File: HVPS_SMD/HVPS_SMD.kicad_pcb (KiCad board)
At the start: 2 copper layers, 36.8 x 22.9 mm, 22 parts, among them J1 CONN_01X02, J2 CONN_01X02, J3 CONN_01X02, Q1 AO4294, T1 WE-FLEX_ER11_5, U1 LM3478SOIC8

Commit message: Prepare for Fab
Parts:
- T1: value WE-FLEX_ER11_5 -> MagTop-HVSMPS
- moved R1 1.92 mm to (183.5, 66.0)
- moved R2 1.78 mm to (185.4, 66.0)
- moved D1 0.48 mm to (194.7, 63.5)
- moved R4 0.31 mm to (183.7, 71.1)
- moved C3 0.18 mm to (188.2, 65.0)
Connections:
- T1 pad 10: Net-(T1-Pad10) -> (no net)
- T1 pad 11: Net-(T1-Pad11) -> (no net)
- T1 pad 12: Net-(T1-Pad12) -> (no net)
- T1 pad 3: Net-(T1-Pad3) -> (no net)
- T1 pad 4: Net-(T1-Pad3) -> (no net)
- T1 pad 6: Net-(T1-Pad12) -> (no net)
- T1 pad 7: Net-(T1-Pad11) -> (no net)
- T1 pad 9: Net-(T1-Pad10) -> (no net)
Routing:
- net Net-(T1-Pad12): track 42.3 -> 0.00 mm
- net GND: track 27.0 -> 40.5 mm
- net Net-(T1-Pad11): track 10.7 -> 0.00 mm
- net Net-(R1-Pad2): track 1.27 -> 2.69 mm
- net Vout: track 13.3 -> 14.7 mm
- net Net-(R2-Pad2): track 28.0 -> 29.3 mm
- net Vin: track 30.6 -> 31.4 mm
- removed copper zone on F.Cu, net Net-(T1-Pad10)
- removed copper zone on F.Cu, net Net-(T1-Pad3)
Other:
- board text added: "nixies.us hvps v0.2"
- board text removed: "nixies.us hvps v0.1"

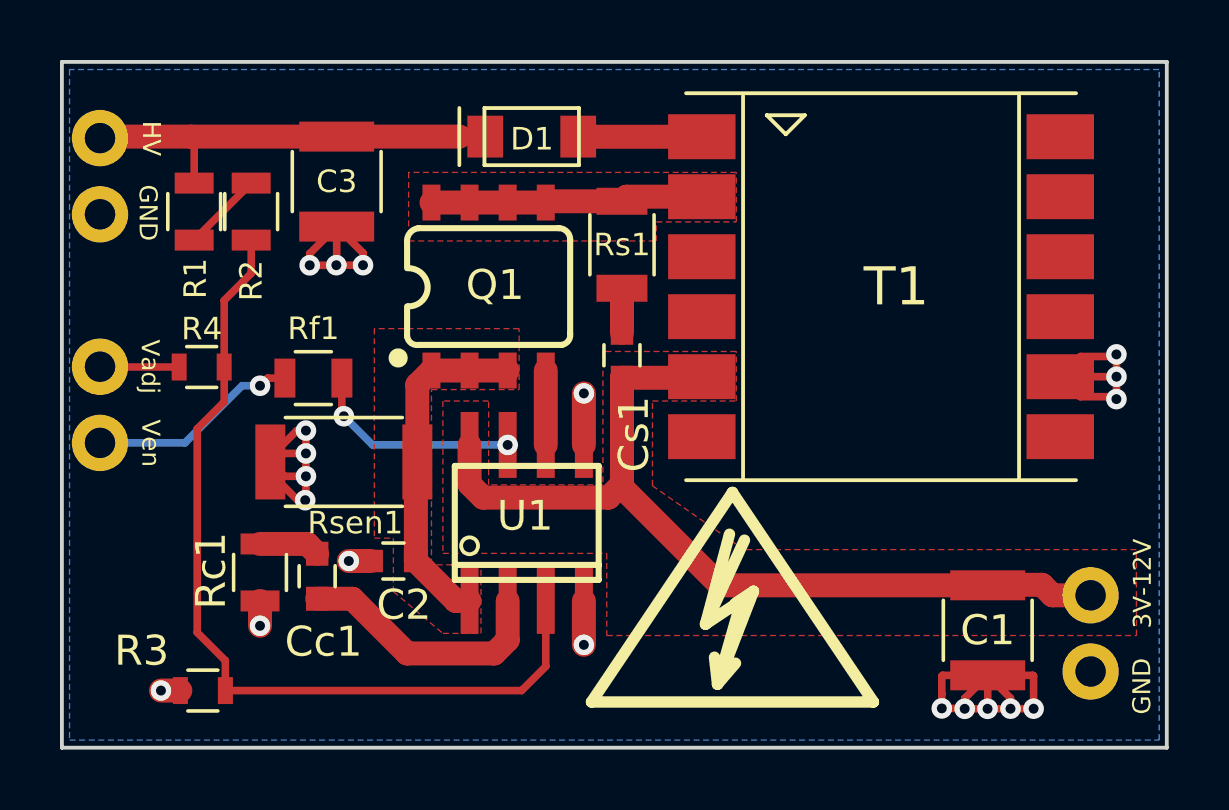
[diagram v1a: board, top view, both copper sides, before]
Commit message: Add footprint for Vfix resistor R5
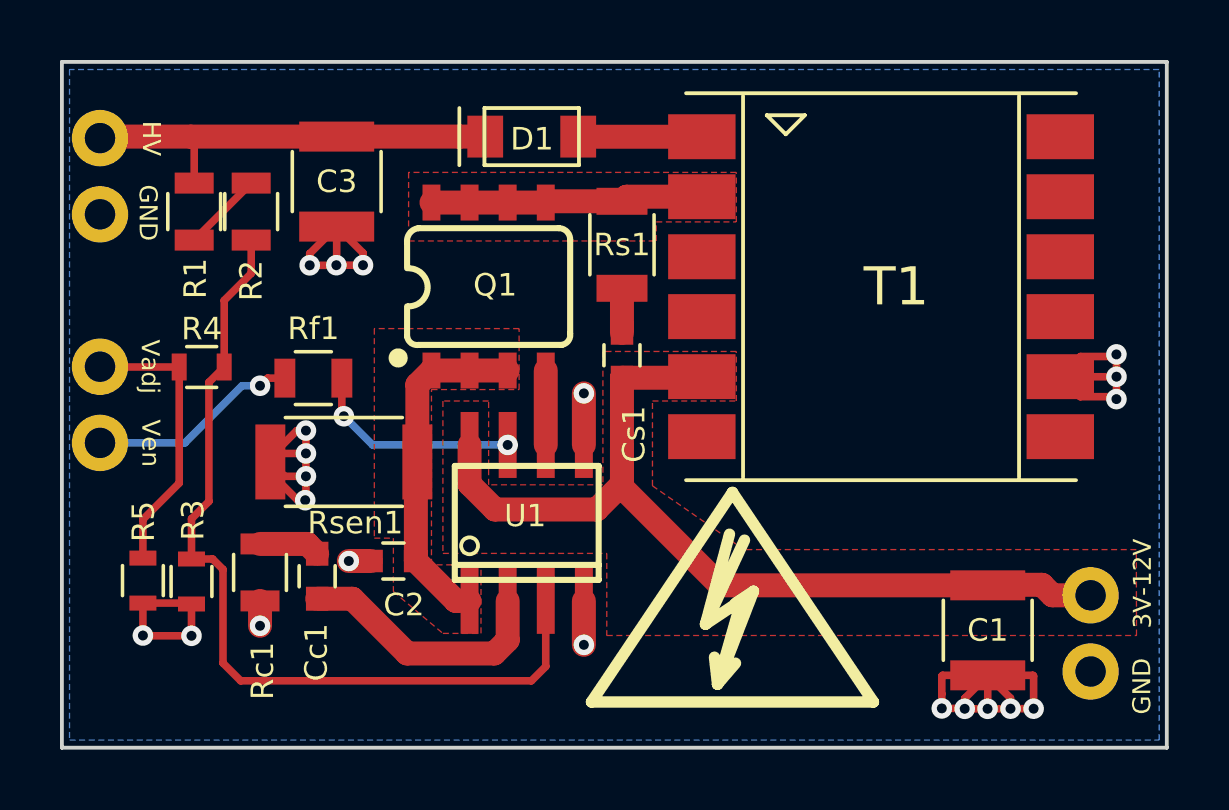
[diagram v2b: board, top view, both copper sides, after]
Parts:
- removed G***: LOGO, logos:mermaid_l
- added R5: 30k, lib_fp:R_0603, F.Cu at (181.8, 78.2)
- moved R3 3.65 mm to (183.4, 78.3), turned to 270 degrees
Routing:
- net Vadj: track 2.64 -> 9.52 mm
- net GND: track 40.5 -> 45.4 mm, vias 20 -> 21

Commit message: Prepare for fab
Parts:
- moved R4 7.39 mm to (181.9, 78.3), turned to 90 degrees
- moved R5 1.39 mm to (180.4, 78.3)
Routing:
- net Vadj: track 9.52 -> 11.5 mm
- net Net-(R2-Pad2): track 29.2 -> 30.7 mm
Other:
- board text added: "nixieclock.biz nixies.us hvps v0.2"
- board text removed: "nixies.us hvps v0.2"
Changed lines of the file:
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@@
     (thickness 1.6002)
     (drawings 11)
-    (tracks 170)
+    (tracks 171)
     (zones 0)
     (modules 22)
@@
   )
   (setup
-    (last_trace_width 0.1524)
+    (last_trace_width 0.254)
     (user_trace_width 0.1524)
     (user_trace_width 0.2)
@@
   )
   (module lib_fp:R_0603 (layer F.Cu)
-    (at 181.77 78.25 90)
+    (at 180.38 78.28 90)
     (descr "Resistor SMD 0603, reflow soldering, Vishay (see dcrcw.pdf)")
     (tags "resistor 0603")
     (attr smd)
-    (fp_text reference R5 (at 1.97 0.02 270) (layer F.SilkS)
+    (fp_text reference R5 (at 1.99 0.03 270) (layer F.SilkS)
       (effects (font (size 0.75 0.75) (thickness 0.1)))
     )
@@
   )
   (module lib_fp:R_0603 (layer F.Cu)
-    (at 183.73 71.13)
+    (at 181.88 78.28 90)
     (descr "Resistor SMD 0603, reflow soldering, Vishay (see dcrcw.pdf)")
     (tags "resistor 0603")
     (attr smd)
-    (fp_text reference R4 (at 0 -1.27 180) (layer F.SilkS)
-      (effects (font (size 0.75 0.75) (thickness 0.1)))
-    )
-    (fp_text value 30k (at 0 1.5) (layer F.Fab)
-      (effects (font (size 1 1) (thickness 0.15)))
-    )
-    (fp_text user %R (at 0 0) (layer F.Fab)
+    (fp_text reference R4 (at 2.01 -0.02 270) (layer F.SilkS)
+      (effects (font (size 0.75 0.75) (thickness 0.1)))
+    )
+    (fp_text value 30k (at 0 1.5 90) (layer F.Fab)
+      (effects (font (size 1 1) (thickness 0.15)))
+    )
+    (fp_text user %R (at 0 0 90) (layer F.Fab)
       (effects (font (size 0.4 0.4) (thickness 0.075)))
     )
@@
     (fp_line (start 1.25 0.7) (end 1.25 -0.7) (layer F.CrtYd) (width 0.05))
     (fp_line (start 1.25 0.7) (end -1.25 0.7) (layer F.CrtYd) (width 0.05))
-    (pad 1 smd rect (at -0.75 0) (size 0.5 0.9) (layers F.Cu F.Paste F.Mask)
+    (pad 1 smd rect (at -0.75 0 90) (size 0.5 0.9) (layers F.Cu F.Paste F.Mask)
       (net 6 Vadj))
-    (pad 2 smd rect (at 0.75 0) (size 0.5 0.9) (layers F.Cu F.Paste F.Mask)
+    (pad 2 smd rect (at 0.75 0 90) (size 0.5 0.9) (layers F.Cu F.Paste F.Mask)
       (net 8 "Net-(R2-Pad2)"))
     (model ${KISYS3DMOD}/Resistors_SMD.3dshapes/R_0603.wrl
@@
     (effects (font (size 0.6 0.6) (thickness 0.127)))
   )
-  (gr_text "nixies.us\nhvps v0.2" (at 204.724 80.645) (layer B.Mask)
+  (gr_text "nixieclock.biz\nnixies.us\nhvps v0.2" (at 207.02 78.95) (layer B.Mask)
     (effects (font (size 1.2 1.2) (thickness 0.254)) (justify left mirror))
   )
@@
   (via (at 189.107 67.736) (size 0.6858) (drill 0.3302) (layers F.Cu B.Cu) (net 2))
   (via (at 188.633009 77.597) (size 0.6858) (drill 0.3302) (layers F.Cu B.Cu) (net 2))
-  (segment (start 185.674 78.928) (end 185.674 79.756) (width 0.8) (layer F.Cu) (net 2))
   (via (at 185.674 79.756) (size 0.6858) (drill 0.3302) (layers F.Cu B.Cu) (net 2))
   (via (at 183.39 80.09) (size 0.6858) (drill 0.3302) (layers F.Cu B.Cu) (net 2))
@@
   (segment (start 189.369 77.597) (end 188.633009 77.597) (width 0.8) (layer F.Cu) (net 2))
   (segment (start 183.36 79) (end 183.39 79.03) (width 0.254) (layer F.Cu) (net 2))
-  (segment (start 181.77 79) (end 183.36 79) (width 0.254) (layer F.Cu) (net 2))
-  (segment (start 185.572 79.03) (end 185.674 78.928) (width 0.254) (layer F.Cu) (net 2))
-  (via (at 181.77 80.08) (size 0.6858) (drill 0.3302) (layers F.Cu B.Cu) (net 2))
-  (segment (start 181.77 79) (end 181.77 80.08) (width 0.254) (layer F.Cu) (net 2))
+  (via (at 180.39 80.09) (size 0.6858) (drill 0.3302) (layers F.Cu B.Cu) (net 2))
   (segment (start 183.39 79.03) (end 183.39 80.09) (width 0.254) (layer F.Cu) (net 2))
-  (segment (start 181.78 80.09) (end 181.77 80.08) (width 0.254) (layer F.Cu) (net 2))
-  (segment (start 183.39 80.09) (end 181.78 80.09) (width 0.254) (layer F.Cu) (net 2))
+  (segment (start 180.38 79.03) (end 180.38 80.08) (width 0.254) (layer F.Cu) (net 2))
+  (segment (start 180.39 80.09) (end 183.39 80.09) (width 0.254) (layer F.Cu) (net 2))
+  (segment (start 185.674 79.756) (end 185.674 78.928) (width 0.254) (layer F.Cu) (net 2))
   (segment (start 192.659 71.247) (end 193.929 71.247) (width 0.8) (layer F.Cu) (net 3))
   (segment (start 191.389 71.247) (end 192.659 71.247) (width 0.8) (layer F.Cu) (net 3))
@@
   (segment (start 185.928 71.501) (end 185.674 71.755) (width 0.254) (layer F.Cu) (net 5))
   (segment (start 186.502 71.501) (end 185.928 71.501) (width 0.254) (layer F.Cu) (net 5))
-  (segment (start 180.35 71.13) (end 180.34 71.12) (width 0.254) (layer F.Cu) (net 6))
-  (segment (start 182.98 71.13) (end 180.35 71.13) (width 0.254) (layer F.Cu) (net 6))
-  (segment (start 181.77 76.21) (end 181.77 77.5) (width 0.254) (layer F.Cu) (net 6))
-  (segment (start 182.98 75) (end 181.77 76.21) (width 0.254) (layer F.Cu) (net 6))
-  (segment (start 182.98 71.13) (end 182.98 75) (width 0.254) (layer F.Cu) (net 6))
+  (segment (start 181.88 78.526) (end 181.88 79.03) (width 0.254) (layer F.Cu) (net 6))
+  (segment (start 181.654 78.3) (end 181.88 78.526) (width 0.254) (layer F.Cu) (net 6))
+  (segment (start 180.646 78.3) (end 181.654 78.3) (width 0.254) (layer F.Cu) (net 6))
+  (segment (start 180.38 78.034) (end 180.646 78.3) (width 0.254) (layer F.Cu) (net 6))
+  (segment (start 180.38 77.53) (end 180.38 78.034) (width 0.254) (layer F.Cu) (net 6))
+  (segment (start 181.77 71.12) (end 180.34 71.12) (width 0.254) (layer F.Cu) (net 6))
+  (segment (start 182.24 71.59) (end 181.77 71.12) (width 0.254) (layer F.Cu) (net 6))
+  (segment (start 182.24 75.166) (end 182.24 71.59) (width 0.254) (layer F.Cu) (net 6))
+  (segment (start 180.38 77.026) (end 182.24 75.166) (width 0.254) (layer F.Cu) (net 6))
+  (segment (start 180.38 77.53) (end 180.38 77.026) (width 0.254) (layer F.Cu) (net 6))
   (segment (start 183.48 66.9) (end 185.38 65) (width 0.254) (layer F.Cu) (net 7))
-  (segment (start 184.48 68.91) (end 184.48 71.13) (width 0.254) (layer F.Cu) (net 8))
-  (segment (start 185.38 68.01) (end 184.48 68.91) (width 0.254) (layer F.Cu) (net 8))
-  (segment (start 185.38 66.9) (end 185.38 68.01) (width 0.254) (layer F.Cu) (net 8))
-  (segment (start 183.39 76.19) (end 183.39 77.53) (width 0.254) (layer F.Cu) (net 8))
-  (segment (start 183.97 75.61) (end 183.39 76.19) (width 0.254) (layer F.Cu) (net 8))
-  (segment (start 183.97 71.64) (end 183.97 75.61) (width 0.254) (layer F.Cu) (net 8))
-  (segment (start 184.48 71.13) (end 183.97 71.64) (width 0.254) (layer F.Cu) (net 8))
   (segment (start 194.72 81.59) (end 195.199 81.111) (width 0.254) (layer F.Cu) (net 8))
   (segment (start 184.44 81) (end 185.03 81.59) (width 0.254) (layer F.Cu) (net 8))
@@
   (segment (start 195.199 81.111) (end 195.199 78.92542) (width 0.254) (layer F.Cu) (net 8))
   (segment (start 183.39 77.53) (end 184.094 77.53) (width 0.254) (layer F.Cu) (net 8))
+  (segment (start 183.39 77.53) (end 181.88 77.53) (width 0.254) (layer F.Cu) (net 8))
+  (segment (start 183.39 76.19) (end 183.39 77.53) (width 0.254) (layer F.Cu) (net 8))
+  (segment (start 183.39 70) (end 183.39 76.19) (width 0.254) (layer F.Cu) (net 8))
+  (segment (start 185.38 68.01) (end 183.39 70) (width 0.254) (layer F.Cu) (net 8))
+  (segment (start 185.38 66.9) (end 185.38 68.01) (width 0.254) (layer F.Cu) (net 8))
   (segment (start 196.28368 63.45428) (end 196.2794 63.45) (width 0.254) (layer F.Cu) (net 9))
   (segment (start 200.40092 63.45428) (end 196.28368 63.45428) (width 0.8) (layer F.Cu) (net 9))
-  (segment (start 185.674 77.028) (end 187.252 77.028) (width 0.8) (layer F.Cu) (net 10))
-  (segment (start 187.252 77.028) (end 187.579 77.355) (width 0.8) (layer F.Cu) (net 10))
-  (segment (start 187.579 78.855) (end 188.754 78.855) (width 0.8) (layer F.Cu) (net 11))
-  (segment (start 188.754 78.855) (end 190.578241 80.679241) (width 0.8) (layer F.Cu) (net 11))
-  (segment (start 190.578241 80.679241) (end 193.481921 80.679241) (width 0.8) (layer F.Cu) (net 11))
-  (segment (start 193.481921 80.679241) (end 193.929 80.232162) (width 0.8) (layer F.Cu) (net 11))
-  (segment (start 193.929 80.232162) (end 193.929 78.92542) (width 0.8) (layer F.Cu) (net 11))
+  (segment (start 186.905 77.355) (end 187.579 77.355) (width 0.254) (layer F.Cu) (net 10))
+  (segment (start 186.578 77.028) (end 186.905 77.355) (width 0.254) (layer F.Cu) (net 10))
+  (segment (start 185.674 77.028) (end 186.578 77.028) (width 0.254) (layer F.Cu) (net 10))
+  (segment (start 193.929 80.251) (end 193.929 78.92542) (width 0.254) (layer F.Cu) (net 11))
+  (segment (start 193.49 80.69) (end 193.929 80.251) (width 0.254) (layer F.Cu) (net 11))
+  (segment (start 188.595 78.855) (end 190.43 80.69) (width 0.254) (layer F.Cu) (net 11))
+  (segment (start 190.43 80.69) (end 193.49 80.69) (width 0.254) (layer F.Cu) (net 11))
+  (segment (start 187.579 78.855) (end 188.595 78.855) (width 0.254) (layer F.Cu) (net 11))
   (segment (start 197.739 68.506) (end 197.739 69.989) (width 0.8) (layer F.Cu) (net 12))
   (via (at 193.929 73.72858) (size 0.6858) (drill 0.3302) (layers F.Cu B.Cu) (net 13))

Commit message: Fab
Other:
- board text added: "v0.2 12/06/2020"
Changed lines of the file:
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@@
   (general
     (thickness 1.6002)
-    (drawings 11)
+    (drawings 12)
     (tracks 171)
     (zones 0)
@@
       (net 1 Vin))
   )
+  (gr_text "v0.2 12/06/2020" (at 208.24 75.98) (layer F.SilkS)
+    (effects (font (size 0.75 0.75) (thickness 0.1)))
+  )
   (gr_text Ven (at 182.03 73.67 270) (layer F.SilkS)

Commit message: More Fab
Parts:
- U1: footprint lib_fp:nixiemisc-SOIC8 -> lib_fp:nixiemisc-SO08
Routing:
- net Net-(Rf1-Pad2): track 7.15 -> 7.88 mm

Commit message: Update Kicad6
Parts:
- removed J3: CONN_01X02, lib_fp:SparkFun-Connectors-1X02_NO_SILK
- removed R2: 604k, lib_fp:R_0805
- removed R4, R5: 30k, lib_fp:R_0603
- removed REF**: Symbol_HighVoltage_Type2_CopperTop_VerySmall, logos:Symbol_HighVoltage_Type2_SilkTop_VerySmall
- removed Rsen1: 0.06, lib_fp:R_2010
- added Rs2: 0.062, lib_fp:R_2010, F.Cu at (187.3, 70.9)
- C2, Cc1, Cs1: footprint lib_fp:C_0603 -> Capacitor_SMD:C_0805_2012Metric
- D1: value ES1FL R3G -> ES1JF; footprint lib_fp:nixiemisc-DO-219AB -> NixieClockMaster:SMAF
- J1, J2: footprint lib_fp:SparkFun-Connectors-1X02_NO_SILK -> NixieClockMaster:Header_MA02-Edge
- Q1, U1: footprint lib_fp:nixiemisc-SO08 -> Package_SO:SOIC-8_3.9x4.9mm_P1.27mm
- R1: value 604k -> 10M
- R3: value 10.2k -> 69.8k; footprint lib_fp:R_0603 -> lib_fp:R_0805
- moved R3 5.27 mm to (186.6, 74.1), turned to 180 degrees
- moved J2 5.00 mm to (183.5, 62.2)
- moved Rf1 3.64 mm to (190.0, 74.1)
- moved Cc1 3.14 mm to (190.0, 76.1), turned to 180 degrees
- moved R1 2.57 mm to (186.0, 65.6)
- moved C1 2.09 mm to (209.7, 77.8)
- moved Rc1 2.09 mm to (186.6, 76.1), turned to 180 degrees
- moved J1 1.14 mm to (213.7, 80.2), turned to -90 degrees
- moved C2 0.52 mm to (190.0, 78.1)
- moved C3 0.50 mm to (188.7, 65.0)
- moved D1 0.48 mm to (194.9, 63.0)
- moved Rs1 0.21 mm to (197.8, 66.9)
- moved Cs1 0.08 mm to (197.8, 70.8)
- turned Q1 to 90 degrees
- turned U1 to 90 degrees
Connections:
- J1 pad 1: GND -> Vin
- J1 pad 2: Vin -> GND
- R3 pad 1: Net-(R2-Pad2) -> Net-(R1-Pad2)
- Rf1 pad 1: Ven -> GND
- T1 pad 1: Net-(D1-PadA) -> Net-(D1-Pad2)
- U1 pad 3: Net-(R2-Pad2) -> Net-(R1-Pad2)
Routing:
- net Net-(R2-Pad2): track 30.7 -> 0.00 mm
- net Net-(R1-Pad2): track 2.69 -> 26.8 mm
- net Vadj: track 11.5 -> 0.00 mm
- net Ven: track 7.06 -> 0.00 mm, vias 1 -> 0
- net Net-(Q1-Pad5): track 9.09 -> 2.55 mm
- net Net-(D1-PadA): track 4.12 -> 0.00 mm
- net Vout: track 14.7 -> 10.7 mm
- net Net-(Cc1-Pad1): track 8.62 -> 4.67 mm
- net Net-(D1-Pad2): track 0.00 -> 3.63 mm
- net Net-(C2-Pad1): track 11.4 -> 14.2 mm
- net Net-(Rf1-Pad2): track 7.88 -> 5.48 mm, vias 2 -> 0
- net GND: track 45.0 -> 47.2 mm, vias 21 -> 23
- net Vin: track 31.7 -> 30.7 mm
- net Net-(Cc1-Pad2): track 2.04 -> 1.50 mm
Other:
- board size 36.8 x 22.9 mm -> 33 x 20 mm
- net class 0.2mm removed
- net class Default removed
- net class Minimal removed
- board text added: "5V"
- board text removed: "3V-12V"
- board text removed: "Vadj"
- board text removed: "Ven"
- board text removed: "nixieclock.biz nixies.us hvps v0.2"
- board text removed: "v0.2 12/06/2020"

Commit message: Shrink
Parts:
- Rs2: footprint lib_fp:R_2010 -> Resistor_SMD:R_1206_3216Metric
- moved R1 4.35 mm to (189.0, 68.8), turned to 0 degrees
- moved J2 3.00 mm to (186.5, 62.2)
- moved Rs2 1.29 mm to (188.6, 70.9)
- moved C3 1.08 mm to (189.7, 64.4)
- moved Q1 0.70 mm to (194.0, 68.4)
- moved D1 0.19 mm to (194.8, 62.9)
- moved Cc1 0.10 mm to (190.1, 76.1)
- moved R3 0.10 mm to (186.7, 74.1)
- moved Rc1 0.10 mm to (186.7, 76.1)
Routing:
- net Net-(R1-Pad2): track 26.8 -> 21.4 mm
- net GND: track 47.2 -> 50.4 mm, vias 23 -> 24
- net Vout: track 10.7 -> 12.7 mm
- net Vin: track 30.7 -> 31.6 mm
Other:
- board size 33 x 20 mm -> 30 x 20 mm

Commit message: More tidy up
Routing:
- net Net-(R1-Pad2): track 21.4 -> 21.9 mm
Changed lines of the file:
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@@
   (segment (start 192.659 78.802) (end 192.302 78.802) (width 0.254) (layer "F.Cu") (net 3))
   (segment (start 190.95 78.1) (end 190.3 78.1) (width 0.254) (layer "F.Cu") (net 3))
-  (segment (start 187.7 66.6) (end 187.7 64.629) (width 0.254) (layer "F.Cu") (net 4))
+  (segment (start 188.05 67.8) (end 187.775 67.525) (width 0.254) (layer "F.Cu") (net 4))
   (segment (start 187.9 62.9) (end 187.371 63.429) (width 0.8) (layer "F.Cu") (net 4))
-  (segment (start 187.5 66.8) (end 187.7 66.6) (width 0.254) (layer "F.Cu") (net 4))
-  (segment (start 188.05 68.15) (end 187.5 67.6) (width 0.254) (layer "F.Cu") (net 4))
-  (segment (start 188.05 68.8) (end 188.05 68.15) (width 0.254) (layer "F.Cu") (net 4))
+  (segment (start 187.775 67.525) (end 187.775 64.025) (width 0.254) (layer "F.Cu") (net 4))
+  (segment (start 188.05 68.8) (end 188.05 67.8) (width 0.254) (layer "F.Cu") (net 4))
+  (segment (start 187.179 63.429) (end 186.5 63.429) (width 0.254) (layer "F.Cu") (net 4))
   (segment (start 192.8 62.9) (end 189.35 62.9) (width 0.8) (layer "F.Cu") (net 4))
-  (segment (start 187.5 67.6) (end 187.5 66.8) (width 0.254) (layer "F.Cu") (net 4))
   (segment (start 189.35 62.9) (end 187.9 62.9) (width 0.8) (layer "F.Cu") (net 4))
-  (segment (start 187.7 64.629) (end 186.5 63.429) (width 0.254) (layer "F.Cu") (net 4))
   (segment (start 187.371 63.429) (end 186.5 63.429) (width 0.8) (layer "F.Cu") (net 4))
+  (segment (start 187.775 64.025) (end 187.179 63.429) (width 0.254) (layer "F.Cu") (net 4))
   (segment (start 187.55 76.1) (end 189.05 76.1) (width 0.254) (layer "F.Cu") (net 5))
   (segment (start 190.95 76.1) (end 192.2 76.1) (width 0.254) (layer "F.Cu") (net 6))
@@
   (segment (start 198.3 62.9) (end 196.8 62.9) (width 0.8) (layer "F.Cu") (net 11))
   (segment (start 200.40092 63.45428) (end 198.85428 63.45428) (width 0.8) (layer "F.Cu") (net 11))
-  (segment (start 187.7 73.95) (end 186.7 74.95) (width 0.254) (layer "F.Cu") (net 12))
-  (segment (start 188.3 70) (end 188.1 70.2) (width 0.254) (layer "F.Cu") (net 12))
+  (segment (start 188.319 69.831) (end 188.081 70.069) (width 0.254) (layer "F.Cu") (net 12))
+  (segment (start 188.808 80.158) (end 194.892 80.158) (width 0.254) (layer "F.Cu") (net 12))
+  (segment (start 195.199 79.851) (end 195.199 78.802) (width 0.254) (layer "F.Cu") (net 12))
+  (segment (start 189.2 69.25) (end 188.619 69.831) (width 0.254) (layer "F.Cu") (net 12))
+  (segment (start 188.081 70.069) (end 188.081 72.719) (width 0.254) (layer "F.Cu") (net 12))
+  (segment (start 187.65 74.1) (end 187.2 74.1) (width 0.254) (layer "F.Cu") (net 12))
+  (segment (start 189.375 68.8) (end 189.2 68.975) (width 0.254) (layer "F.Cu") (net 12))
+  (segment (start 187.65 73.15) (end 187.65 74.1) (width 0.254) (layer "F.Cu") (net 12))
+  (segment (start 187.2 74.1) (end 186.7 74.6) (width 0.254) (layer "F.Cu") (net 12))
+  (segment (start 189.2 68.975) (end 189.2 69.25) (width 0.254) (layer "F.Cu") (net 12))
   (segment (start 186.7 78.05) (end 188.808 80.158) (width 0.254) (layer "F.Cu") (net 12))
-  (segment (start 195.199 79.851) (end 195.199 78.802) (width 0.254) (layer "F.Cu") (net 12))
-  (segment (start 188.808 80.158) (end 194.892 80.158) (width 0.254) (layer "F.Cu") (net 12))
-  (segment (start 188.75 70) (end 188.3 70) (width 0.254) (layer "F.Cu") (net 12))
-  (segment (start 186.7 74.95) (end 186.7 78.05) (width 0.254) (layer "F.Cu") (net 12))
-  (segment (start 189.95 68.8) (end 188.75 70) (width 0.254) (layer "F.Cu") (net 12))
-  (segment (start 188.1 72.7) (end 187.7 73.1) (width 0.254) (layer "F.Cu") (net 12))
-  (segment (start 188.1 70.2) (end 188.1 72.7) (width 0.254) (layer "F.Cu") (net 12))
   (segment (start 194.892 80.158) (end 195.199 79.851) (width 0.254) (layer "F.Cu") (net 12))
-  (segment (start 187.7 73.1) (end 187.7 73.95) (width 0.254) (layer "F.Cu") (net 12))
+  (segment (start 189.95 68.8) (end 189.375 68.8) (width 0.254) (layer "F.Cu") (net 12))
+  (segment (start 186.7 74.6) (end 186.7 78.05) (width 0.254) (layer "F.Cu") (net 12))
+  (segment (start 188.619 69.831) (end 188.319 69.831) (width 0.254) (layer "F.Cu") (net 12))
+  (segment (start 188.081 72.719) (end 187.65 73.15) (width 0.254) (layer "F.Cu") (net 12))
   (zone (net 9) (net_name "Net-(Q1-Pad5)") (layer "F.Cu") (hatch edge 0.508)
     (connect_pads yes (clearance 0.1524))
